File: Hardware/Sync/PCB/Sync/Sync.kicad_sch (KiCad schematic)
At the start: 14 parts, among them J1 Conn_01x04_Male, J2 Conn_01x02_Pin, J3 AudioJack3, J4 AudioJack3, Q1 2N3904, Q2 2N3904

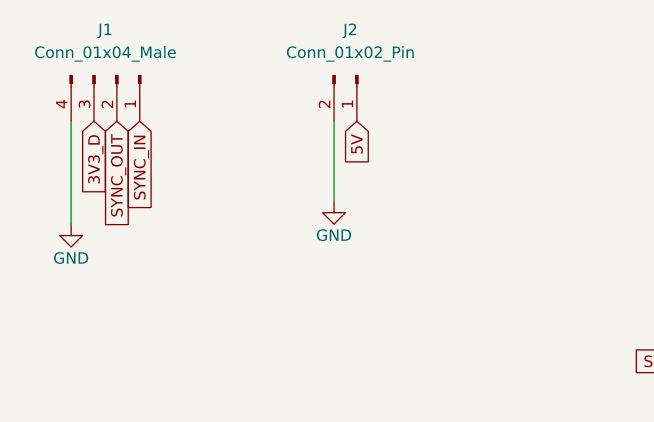
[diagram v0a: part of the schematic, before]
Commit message: Edges removed
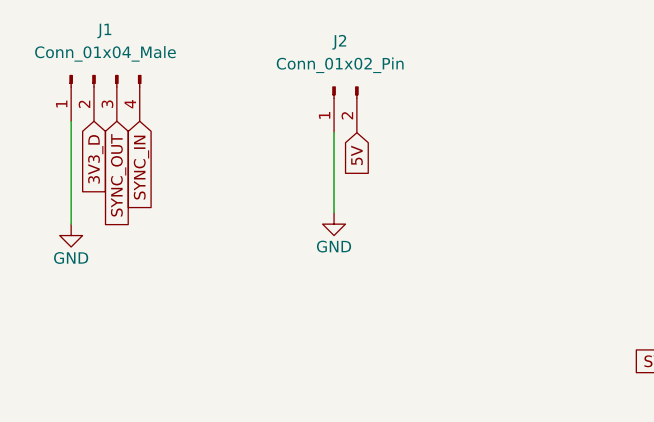
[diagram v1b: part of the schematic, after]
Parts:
- J1: footprint Connector_PinSocket_2.54mm:PinSocket_1x04_P2.54mm_Vertical -> Connector_PinHeader_2.54mm:PinHeader_1x04_P2.54mm_Horizontal
- J2: footprint Connector_PinSocket_2.54mm:PinSocket_1x02_P2.54mm_Vertical -> Connector_PinHeader_2.54mm:PinHeader_1x02_P2.54mm_Horizontal
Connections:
- net 3V3_D: now also J1.2 (Pin_2); no longer J1.3 (Pin_3)
- net 5V: now also J2.2 (Pin_2); no longer J2.1 (Pin_1)
- net GND: now also J1.1 (Pin_1), J2.1 (Pin_1); no longer J1.4 (Pin_4), J2.2 (Pin_2)
- net SYNC_IN: now also J1.4 (Pin_4); no longer J1.1 (Pin_1)
- net SYNC_OUT: now also J1.3 (Pin_3); no longer J1.2 (Pin_2)
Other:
- moved on the sheet: J1, J2
